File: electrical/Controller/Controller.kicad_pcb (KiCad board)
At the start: 2 copper layers, 30 x 45 mm, 48 parts, among them J1 USB4105-GF-A, J4 TC2030-NL, U1 USBLC6-2P6, U2 LP5912-3.3DRV, U3 W25Q16JVUXIQ, U4 RP2040, U5 ABPMRRV001PD2A3, Y1 12 MHz

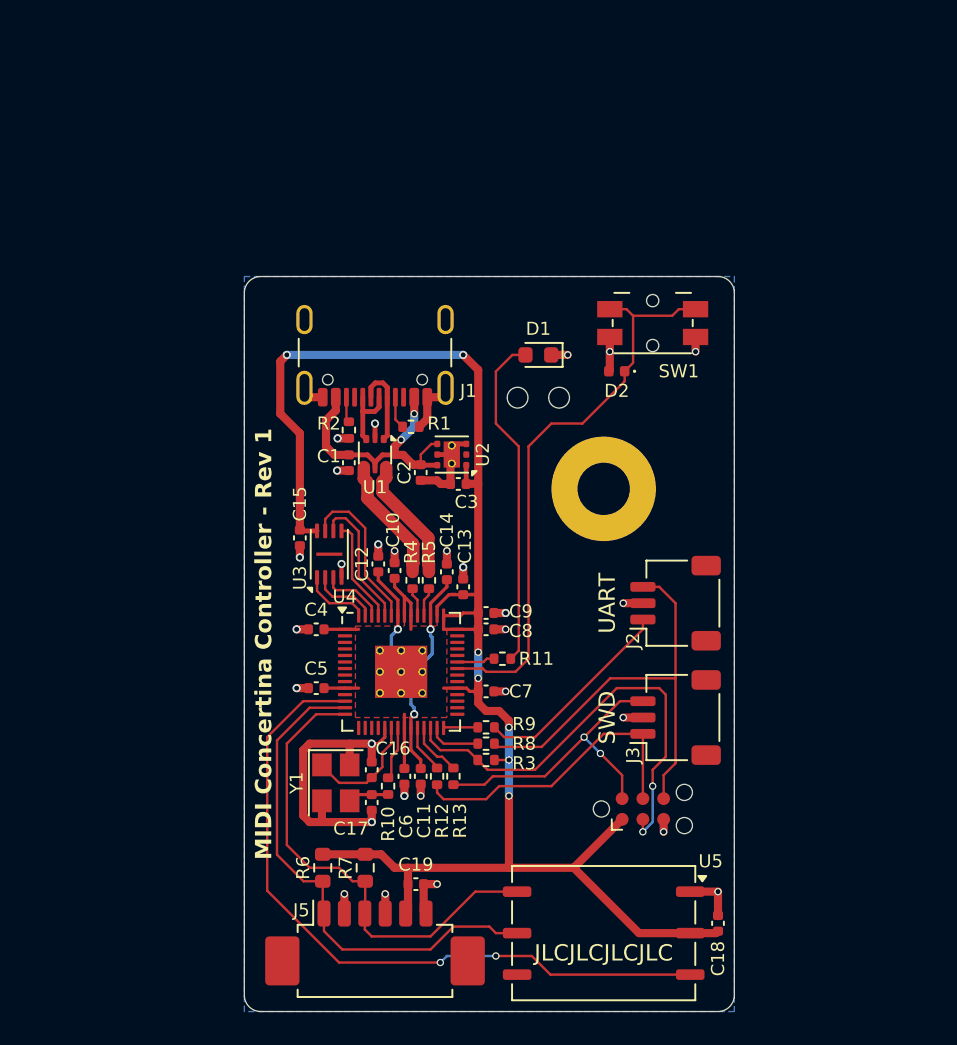
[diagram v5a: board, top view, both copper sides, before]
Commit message: Redesign controller schematic with STM32
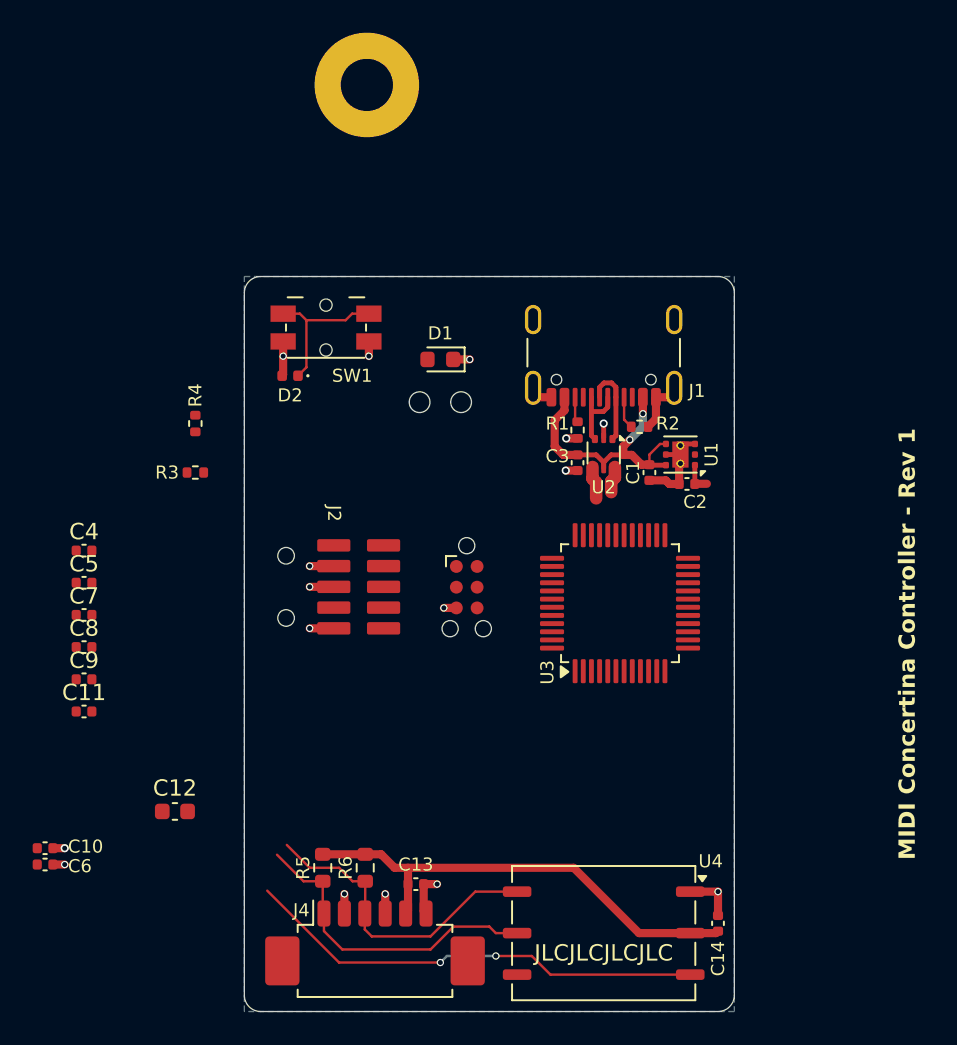
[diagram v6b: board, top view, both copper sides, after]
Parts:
- removed the C10 at (139.2, 88.0)
- removed the C13 at (143.4, 89.0)
- removed the C14 at (142.4, 88.1)
- removed C15: 100n, Capacitor_SMD:C_0402_1005Metric
- removed C16, C17: 15p, Capacitor_SMD:C_0402_1005Metric
- removed the C6 at (139.8, 100.6)
- removed the J3 at (156.4, 97.0)
- removed R10: 1k, Resistor_SMD:R_0402_1005Metric
- removed R12, R13, R8, R9: 100R, Resistor_SMD:R_0402_1005Metric
- removed the R4 at (140.3, 88.6)
- removed the R5 at (141.3, 88.6)
- removed the U4 at (139.6, 94.2)
- removed Y1: 12 MHz, Crystal:Crystal_SMD_3225-4Pin_3.2x2.5mm
- added C8: 100nF, Capacitor_SMD:C_0402_1005Metric, F.Cu at (120.2, 92.7)
- added C9: 100nF, Capacitor_SMD:C_0402_1005Metric, F.Cu at (120.2, 94.7)
- C10: renamed from C9; value 100n -> 100nF
- C11, C7: value 100n -> 100nF
- C12: value 100n -> 10uF; footprint Capacitor_SMD:C_0402_1005Metric -> Capacitor_SMD:C_0603_1608Metric
- C4, C5: value 100n -> 1uF
- C6: renamed from C8; value 100n -> 100nF
- J2: value ~ -> SWD_10; footprint Connector_JST:JST_SH_SM03B-SRSS-TB_1x03-1MP_P1.00mm_Horizontal -> MidiConcertina:Samtech_FTSH-105-01-L-DH
- R3: value 1k -> 47k
- U3: value W25Q16JVUXIQ -> STM32L072CBTx; footprint Package_SON:Winbond_USON-8-1EP_3x2mm_P0.5mm_EP0.2x1.6mm -> Package_QFP:LQFP-48_7x7mm_P0.5mm
- moved C10 30.6 mm to (117.8, 105.0)
- moved C6 30.6 mm to (117.8, 106.0)
- moved H2 28.7 mm to (137.5, 58.3)
- moved C7 25.1 mm to (120.2, 90.7)
- moved R3 25.0 mm to (127.0, 82.0)
- moved R4 23.7 mm to (127.0, 79.0), turned to 90 degrees
- moved C11 21.0 mm to (120.2, 96.6), turned to 0 degrees
- moved D2 20.0 mm to (132.8, 76.1)
- moved SW1 20.0 mm to (135.0, 73.1)
- moved C12 19.6 mm to (125.8, 102.8), turned to 0 degrees
- moved J2 19.4 mm to (137.0, 89.0), turned to -90 degrees
- moved U3 18.1 mm to (153.0, 90.0)
- moved J3 17.3 mm to (143.6, 89.0), turned to -90 degrees
- moved C5 15.6 mm to (120.2, 88.8), turned to 0 degrees
- moved C4 15.0 mm to (120.2, 86.8), turned to 0 degrees
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- renumbered C2 to C1, C19 to C13, C18 to C14, C3 to C2, C1 to C3, H2 to H1, H1 to H2, J4 to J3, J5 to J4, R2 to R1, R1 to R2, R11 to R4, R6 to R5, R7 to R6, U2 to U1, U1 to U2, U5 to U4
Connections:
- C10 pad 1: +3.3V -> NRST
- C11 pad 1: +1V1 -> +3.3V
- C12 pad 1: +1V1 -> +3.3V
- J2 pad 1: UART_RX -> +3.3V
- J2 pad 2: GND -> /SWDIO
- J2 pad 3: UART_TX -> GND
- J3 pad 2: SWDIO -> /SWDIO
- J3 pad 3: RUN -> NRST
- J3 pad 4: SWCLK -> /SWCLK
- J4 pad 1: I2C_SDA -> /I2C_SDA
- J4 pad 3: I2C_SCL -> /I2C_SCL
- R3 pad 1: +3.3V -> Net-(U3-BOOT0)
- R3 pad 2: RUN -> GND
- R4 pad 1: Net-(U4-GPIO25) -> Net-(U3-PB5)
- R5 pad 2: I2C_SDA -> /I2C_SCL
- R6 pad 2: I2C_SCL -> /I2C_SDA
- U2 pad 4: USB_D+ -> /USB_D+
- U2 pad 6: USB_D- -> /USB_D-
- U3 pad 1: /QSPI_SS -> +3.3V
- U3 pad 2: /QSPI_SD1 -> unconnected-(U3-PC13-Pad2)
- U3 pad 3: /QSPI_SD2 -> unconnected-(U3-PC14-Pad3)
- U3 pad 4: GND -> unconnected-(U3-PC15-Pad4)
- U3 pad 5: /QSPI_SD0 -> unconnected-(U3-PH0-Pad5)
- U3 pad 6: /QSPI_SCLK -> unconnected-(U3-PH1-Pad6)
- U3 pad 7: /QSPI_SD3 -> NRST
- U3 pad 8: +3.3V -> GND
- U3 pad 9: (no net) -> +3.3V
- U4 pad 3: PRESSURE_INT -> unconnected-(U4-INT-Pad3)
- U4 pad 5: I2C_SDA -> /I2C_SDA
- U4 pad 6: I2C_SCL -> /I2C_SCL
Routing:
- net +3.3V: track 115.4 -> 31.0 mm, vias 7 -> 0
- net PRESSURE_INT: track 43.4 -> 0.00 mm, vias 2 -> 0
- net (no net): track 0.00 -> 38.9 mm
- net I2C_SDA: track 31.6 -> 0.00 mm
- net I2C_SCL: track 29.8 -> 0.00 mm
- net unconnected-(U4-INT-Pad3): track 0.00 -> 28.4 mm, vias 0 -> 2
- net RUN: track 27.9 -> 0.00 mm, vias 2 -> 0
- net UART_TX: track 27.6 -> 0.00 mm
- net Net-(D2-K): track 35.1 -> 9.19 mm
- net GND: track 56.2 -> 31.4 mm, vias 28 -> 16
- net Net-(D1-A): track 20.6 -> 0.00 mm
- net +1V1: track 20.6 -> 0.00 mm, vias 3 -> 0
- net SWCLK: track 18.9 -> 0.00 mm
- net SWDIO: track 18.4 -> 0.00 mm, vias 2 -> 0
- net UART_RX: track 12.7 -> 0.00 mm
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- removed copper zone on F.Cu, net +3.3V
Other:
- board text removed: "SWD"
- board text removed: "UART"

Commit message: Layout controller PCB with STM32 and updated connector pinout
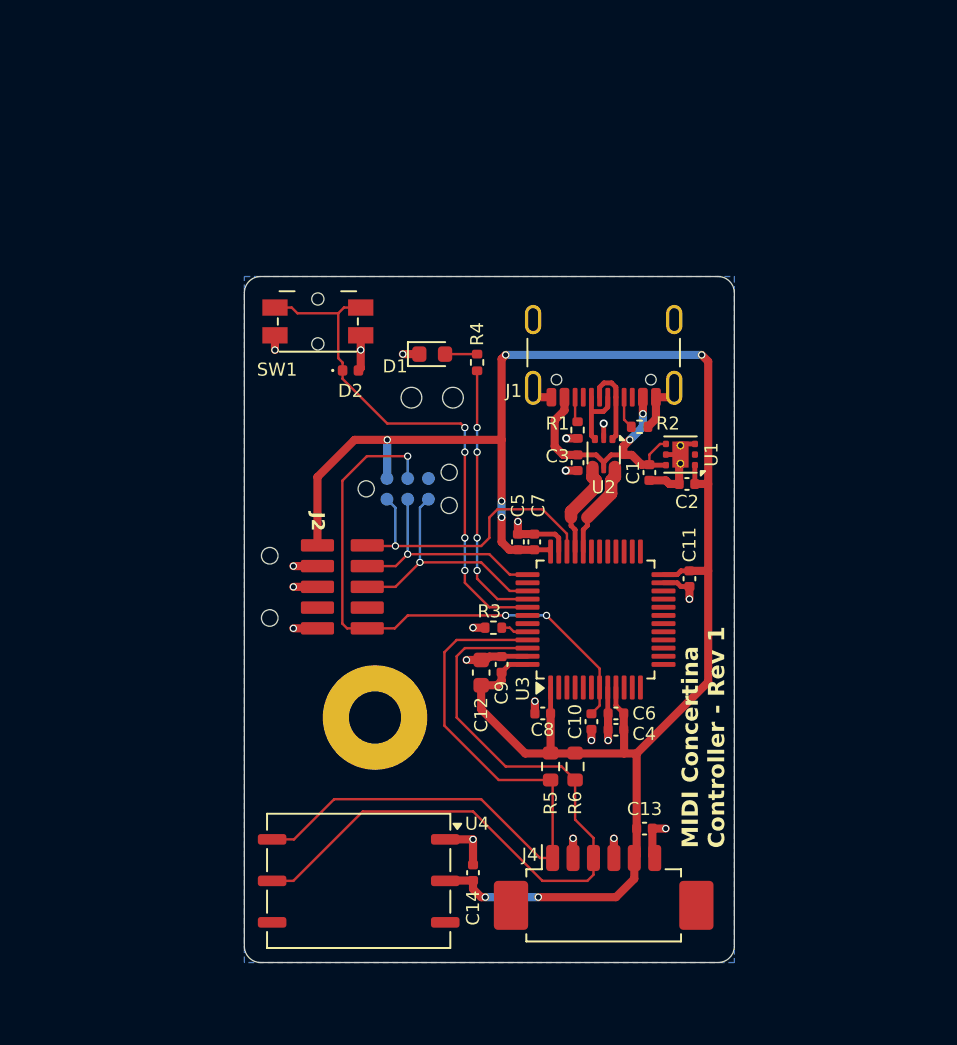
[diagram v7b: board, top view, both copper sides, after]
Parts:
- J3: moved to B.Cu
- moved H2 38.7 mm to (138.0, 97.0)
- moved C11 37.9 mm to (157.2, 88.5), turned to -90 degrees
- moved C6 36.2 mm to (152.8, 96.8), turned to 180 degrees
- moved C4 34.4 mm to (152.8, 97.8), turned to 180 degrees
- moved C10 34.3 mm to (151.2, 97.2), turned to -90 degrees
- moved C8 28.4 mm to (148.3, 96.8), turned to 180 degrees
- moved C7 27.9 mm to (147.8, 86.2), turned to 90 degrees
- moved C5 26.7 mm to (146.8, 86.2), turned to 90 degrees
- moved C9 25.6 mm to (145.8, 93.8), turned to 90 degrees
- moved C12 20.6 mm to (144.5, 94.2), turned to 90 degrees
- moved R3 20.6 mm to (145.2, 91.5)
- moved R4 17.7 mm to (144.2, 75.3)
- moved U4 15.3 mm to (137.0, 107.0)
- moved C14 15.3 mm to (144.0, 106.5)
- moved R5 15.3 mm to (148.8, 100.0)
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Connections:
- J4 pad 1: /I2C_SDA -> /I2C_SCL
- J4 pad 3: /I2C_SCL -> /I2C_SDA
- R4 pad 1: Net-(U3-PB5) -> Net-(U3-PB4)
- U3 pad 40: Net-(D2-K) -> Net-(U3-PB4)
- U3 pad 41: Net-(U3-PB5) -> Net-(D2-K)
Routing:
- net +3.3V: track 31.0 -> 121.3 mm, vias 0 -> 7
- net /I2C_SDA: track 0.00 -> 46.7 mm
- net /I2C_SCL: track 0.00 -> 42.3 mm
- net (no net): track 38.9 -> 0.00 mm
- net NRST: track 0.00 -> 35.3 mm, vias 0 -> 3
- net unconnected-(U4-INT-Pad3): track 28.4 -> 0.00 mm, vias 2 -> 0
- net Net-(D2-K): track 9.19 -> 32.3 mm, vias 0 -> 4
- net /SWDIO: track 0.00 -> 18.7 mm, vias 0 -> 1
- net Net-(U3-PB4): track 0.00 -> 16.3 mm, vias 0 -> 4
- net UART_TX: track 0.00 -> 15.2 mm, vias 0 -> 1
- net /SWCLK: track 0.00 -> 14.0 mm, vias 0 -> 1
- net GND: track 31.4 -> 45.2 mm, vias 16 -> 20
- net /USB_D-: track 1.63 -> 5.98 mm
- net /USB_D+: track 2.01 -> 6.01 mm
- net Net-(D1-A): track 0.00 -> 1.96 mm
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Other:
- board size 30 x 45 mm -> 30 x 42 mm
- board text removed: "JLCJLCJLCJLC"

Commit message: PCB adjustments
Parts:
- H2: footprint MountingHole:MountingHole_3.2mm_M3_Pad -> MountingHole:MountingHole_3.2mm_M3
- moved C13 1.00 mm to (154.5, 104.8)
- moved J4 1.00 mm to (152.0, 109.0)
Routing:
- net /I2C_SDA: track 46.7 -> 39.4 mm, vias 0 -> 2
- net /I2C_SCL: track 42.3 -> 37.4 mm
- net +3.3V: track 121.3 -> 121.8 mm, vias 7 -> 5
